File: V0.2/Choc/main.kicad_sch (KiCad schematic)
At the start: 41 parts, among them J1 Conn_01x02_Female, J1 USB_C_2.0, SW1 SW_DPST_x2, SW10 SW_DPST_x2, SW11 SW_DPST_x2, SW12 SW_DPST_x2, SW13 SW_DPST_x2, SW14 SW_DPST_x2, SW15 SW_DPST_x2, SW16 SW_DPST_x2, SW17 SW_DPST_x2, SW18 SW_DPST_x2, SW19 SW_DPST_x2, SW2 SW_DPST_x2, SW20 SW_DPST_x2, SW21 SW_DPST_x2, SW3 SW_DPST_x2, SW4 SW_DPST_x2, SW5 SW_DPST_x2, SW6 SW_DPST_x2, SW7 SW_DPST_x2, SW8 SW_DPST_x2, SW9 SW_DPST_x2, U1 E73-2G4M08S1E, X1 32.768kHz

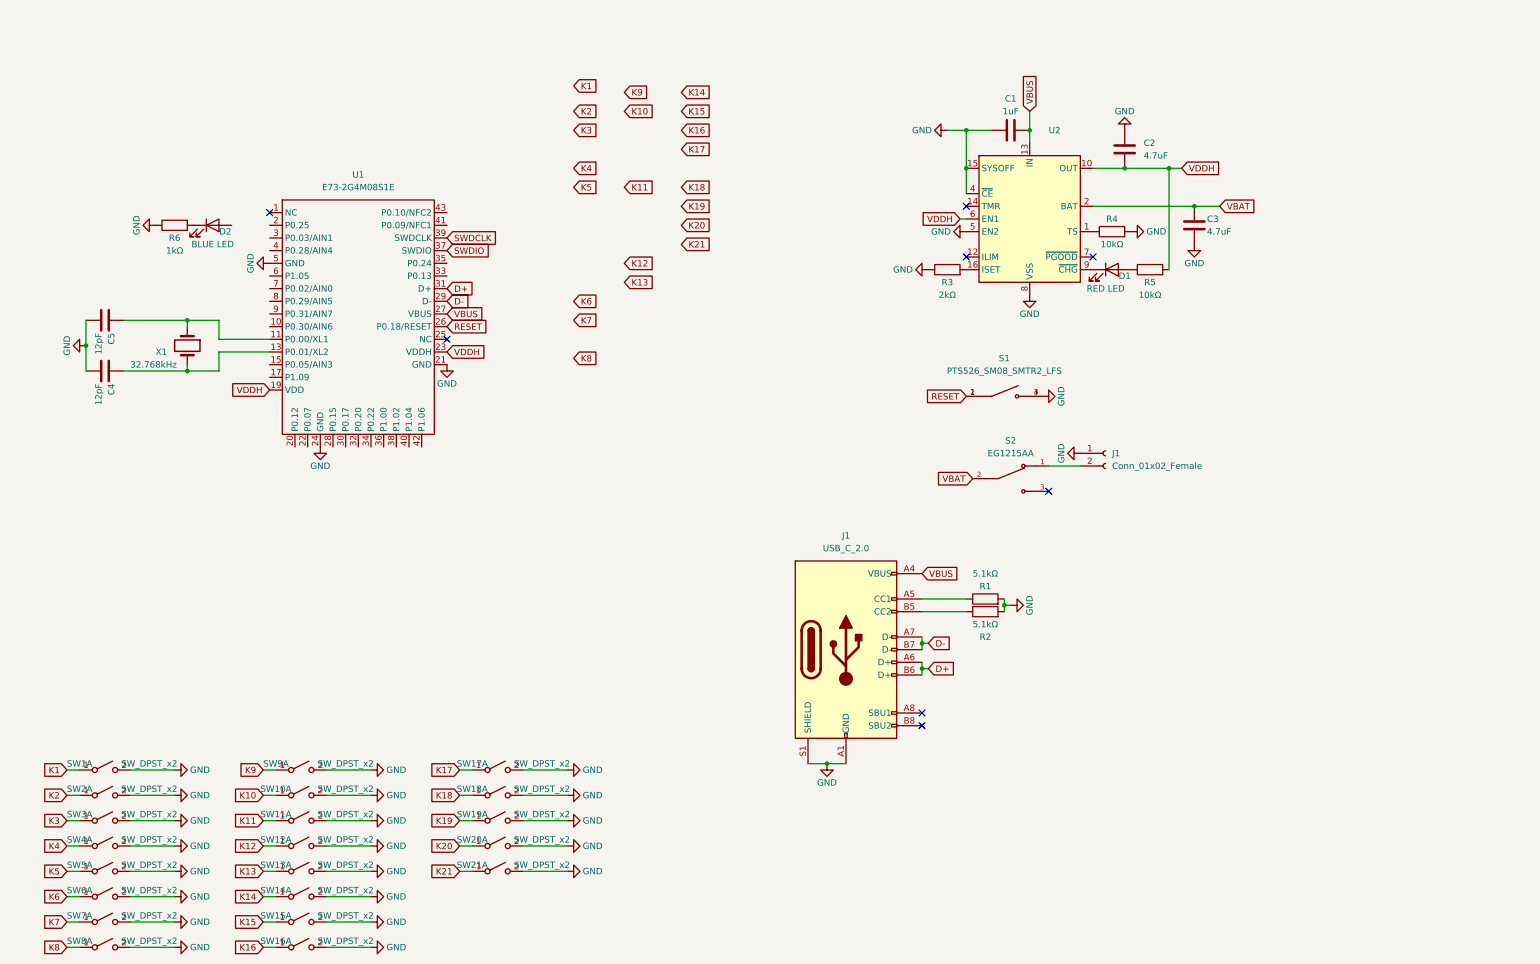
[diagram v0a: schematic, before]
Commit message: Just need to change ESD
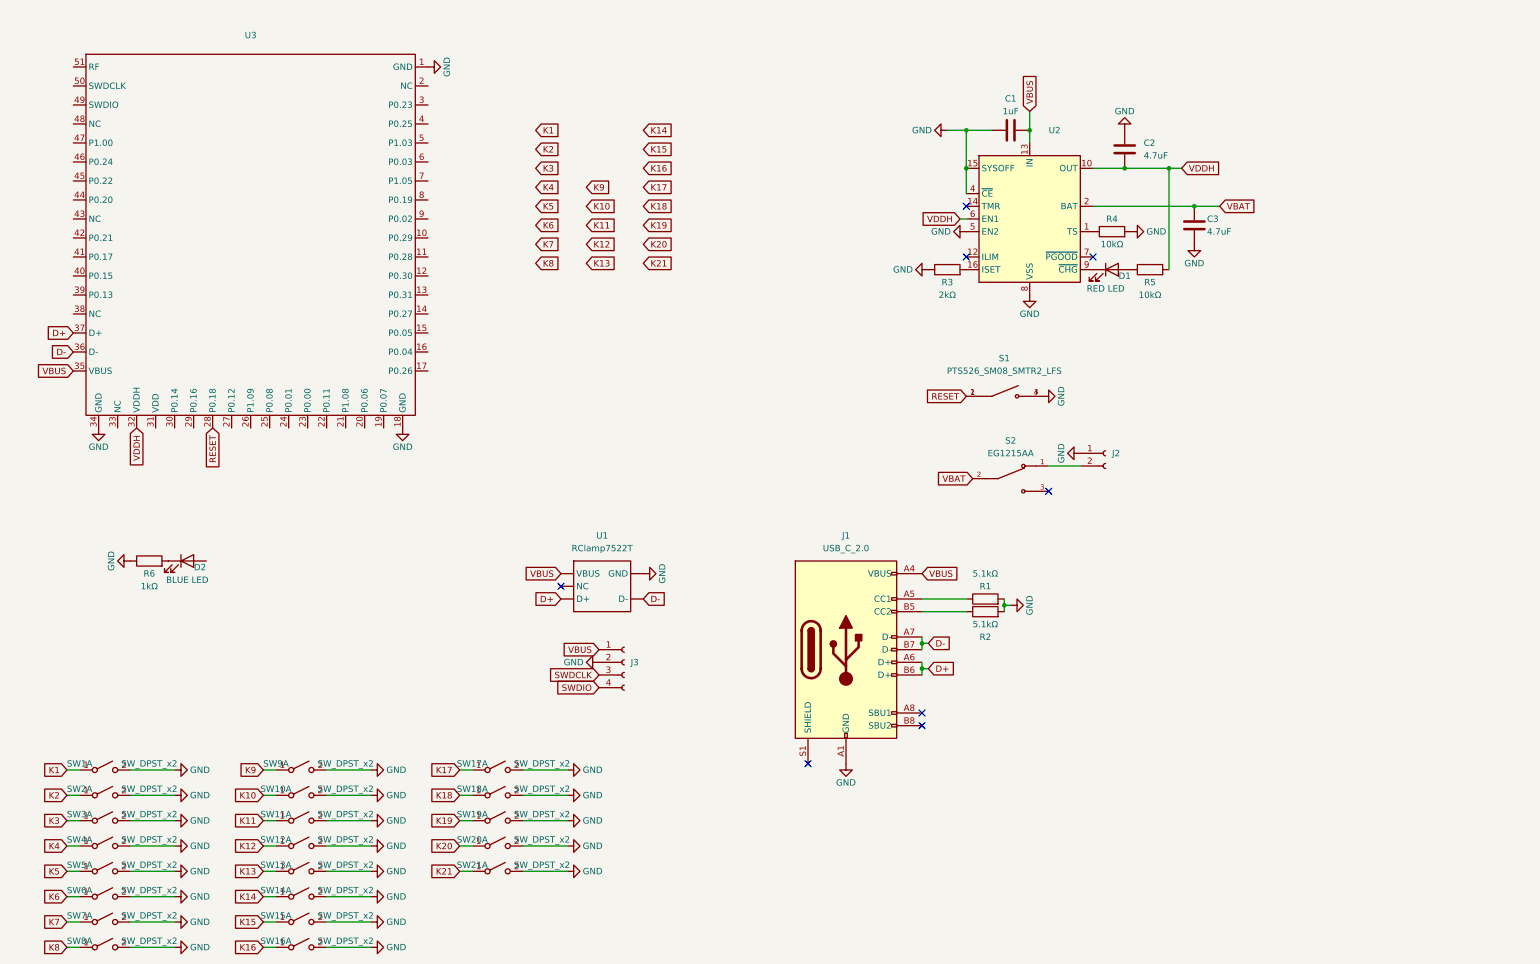
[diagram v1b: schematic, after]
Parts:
- removed C4, C5: 12pF, symbol Device:C
- removed U1: E73-2G4M08S1E, symbol E73-2G4M08S1E:E73-2G4M08S1E
- removed X1: 32.768kHz, symbol Device:Crystal
- added J3: (no value), symbol Connector:Conn_01x04_Female
- added U1: RClamp7522T, symbol Semtech:RClamp7522T
- added U3: (no value), symbol 0_ARognes:MS88SF31_Min
- J2: renamed from J1; value Conn_01x02_Female -> (none)
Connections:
- net D+: now also U1. (VBUS), U3.37 (D+)
- net D-: now also U1. (VBUS), U3.36 (D-)
- net GND: now also J3.2 (Pin_2), U1. (VBUS), U3.1 (GND), U3.18 (GND), U3.34 (GND); no longer J1.S1 (SHIELD)
- net RESET: now also U3.28 (P0.18)
- net SWDCLK: now also J3.3 (Pin_3)
- net SWDIO: now also J3.4 (Pin_4)
- net VBUS: now also J3.1 (Pin_1), U1. (VBUS), U3.35 (VBUS)
- net VDDH: now also U3.32 (VDDH)
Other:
- title: (none) -> Estoc

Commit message: Difficult circuitry complete, just wire
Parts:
- removed U1: RClamp7522T, symbol Semtech:RClamp7522T
- added U1: IP4234CZ6, symbol Nexperia:IP4234CZ6
- J2: value (none) -> JST-BAT
- J3: value (none) -> SWD
- U2: value (none) -> BQ24072; footprint (none) -> Package_DFN_QFN:VQFN-16-1EP_3x3mm_P0.5mm_EP1.6x1.6mm
- U3: value (none) -> MS88SF31_Min
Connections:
- net D+: now also U1.3 (ESD); no longer U3.37 (D+)
- net D-: now also U1.4 (ESD); no longer U3.36 (D-)
- net GND: now also U1.2 (GND)
- net SWDCLK: now also U3.50 (SWDCLK)
- net SWDIO: now also U3.49 (SWDIO)
- net VBUS: now also U1.5 (VBUS)
- net STATUS: now reaches D2.2 (A)
- new net D+ESD: U1.1 (ESD), U3.37 (D+)
- new net D-ESD: U1.6 (ESD), U3.36 (D-)
- no-connect marks 8 -> 14

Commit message: Update Readme
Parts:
- added C4: 1uF, symbol Device:C
- added C5, C6: 4.7uF, symbol Device:C
- added D3: RED LED, symbol Device:LED
- added D4: BLUE LED, symbol Device:LED
- added J4: USB_C_2.0, symbol Connector:USB_C_Receptacle_USB2.0
- added J5: JST-BAT, symbol Connector:Conn_01x02_Female
- added J6: SWD, symbol Connector:Conn_01x04_Female
- added R10, R11: 10kΩ, symbol Device:R
- added R12: 1kΩ, symbol Device:R
- added R7, R8: 5.1kΩ, symbol Device:R
- added R9: 2kΩ, symbol Device:R
- added S3: (no value), SW_PTS526_SM08_SMTR2_LFS, symbol PTS526_SM08_SMTR2_LFS:PTS526_SM08_SMTR2_LFS
- added S4: EG1215AA, SW_EG1215AA, symbol EG1215AA:EG1215AA
- added SW22, SW23, SW24, SW25, SW26, SW27, SW28, SW29, SW30, SW31, SW32, SW33, SW34, SW35, SW36, SW37, SW38, SW39, SW40, SW41, SW42: SW_DPST_x2, symbol Switch:SW_DPST_x2
- added U4: MS88SF31_Min, symbol 0_ARognes:MS88SF31_Min
- added U5: BQ24072, Package_DFN_QFN:VQFN-16-1EP_3x3mm_P0.5mm_EP1.6x1.6mm, symbol Battery_Management:BQ24075RGT
- added U6: IP4234CZ6, symbol Nexperia:IP4234CZ6
- S1: value PTS526_SM08_SMTR2_LFS -> (none)
- renumbered U3 to U1, U1 to U3
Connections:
- net D+: now also J4.A6 (D+), J4.B6 (D+), U6.3 (ESD)
- net D+ESD: now also U4.37 (D+), U6.1 (ESD)
- net D-: now also J4.A7 (D-), J4.B7 (D-), U6.4 (ESD)
- net D-ESD: now also U4.36 (D-), U6.6 (ESD)
- net GND: now also C4.1, C5.2, C6.1, J4.A1 (GND), J4.A12 (GND), J4.B1 (GND), J4.B12 (GND), J5.1 (Pin_1), J6.2 (Pin_2), R10.2, R12.1, R7.2, R8.2, R9.1, S3.3, S3.4, SW22.2 (B), SW23.2 (B), SW24.2 (B), SW25.2 (B), SW26.2 (B), SW27.2 (B), SW28.2 (B), SW29.2 (B), SW30.2 (B), SW31.2 (B), SW32.2 (B), SW33.2 (B), SW34.2 (B), SW35.2 (B), SW36.2 (B), SW37.2 (B), SW38.2 (B), SW39.2 (B), SW40.2 (B), SW41.2 (B), SW42.2 (B), U4.1 (GND), U4.18 (GND), U4.34 (GND), U5.15 (SYSOFF), U5.17 (VSS), U5.4 (~{CE}), U5.5 (EN2), U5.8 (VSS), U6.2 (GND)
- net K1: now also U1.23 (P0.00), SW22.1 (A), U4.20 (P0.06)
- net K10: now also U1.29 (P0.16), SW31.1 (A), U4.11 (P0.28)
- net K11: now also U1.40 (P0.15), SW32.1 (A), U4.10 (P0.29)
- net K12: now also U1.44 (P0.20), SW33.1 (A), U4.3 (P0.23)
- net K13: now also U1.20 (P0.06), SW34.1 (A), U4.25 (P0.08)
- net K14: now also U1.19 (P0.07), SW35.1 (A), U4.39 (P0.13)
- net K15: now also U1.16 (P0.04), SW36.1 (A), U4.40 (P0.15)
- net K16: now also U1.15 (P0.05), SW37.1 (A), U4.41 (P0.17)
- net K17: now also U1.24 (P0.01), SW38.1 (A), U4.42 (P0.21)
- net K18: now also U1.39 (P0.13), SW39.1 (A), U4.5 (P1.03)
- net K19: now also U1.5 (P1.03), SW40.1 (A), U4.45 (P0.22)
- net K2: now also U1.26 (P1.09), SW23.1 (A), U4.21 (P1.08)
- net K20: now also U1.4 (P0.25), SW41.1 (A), U4.46 (P0.24)
- net K21: now also U1.3 (P0.23), SW42.1 (A), U4.47 (P1.00)
- net K3: now also U1.27 (P0.12), SW24.1 (A), U4.13 (P0.31)
- net K4: now also U1.30 (P0.14), SW25.1 (A), U4.12 (P0.30)
- net K5: now also U1.41 (P0.17), SW26.1 (A), U4.9 (P0.02)
- net K6: now also U1.42 (P0.21), SW27.1 (A), U4.4 (P0.25)
- net K7: now also U1.22 (P0.11), SW28.1 (A), U4.23 (P0.00)
- net K8: now also U1.21 (P1.08), SW29.1 (A), U4.24 (P0.01)
- net K9: now also U1.25 (P0.08), SW30.1 (A), U4.22 (P0.11)
- net RESET: now also S3.1, S3.2, U4.28 (P0.18)
- net STATUS: now also U1.17 (P0.26), D4.2 (A), U4.17 (P0.26)
- net SWDCLK: now also J6.3 (Pin_3), U4.50 (SWDCLK)
- net SWDIO: now also J6.4 (Pin_4), U4.49 (SWDIO)
- net VBAT: now also C6.2, S4.2, U5.2 (BAT), U5.3 (BAT)
- net VBUS: now also C4.2, J4.A4 (VBUS), J4.A9 (VBUS), J4.B4 (VBUS), J4.B9 (VBUS), J6.1 (Pin_1), U4.35 (VBUS), U5.13 (IN), U6.5 (VBUS)
- net VDDH: now also C5.1, R11.2, U4.32 (VDDH), U5.10 (OUT), U5.11 (OUT), U5.6 (EN1)
- new net: J5.2 (Pin_2), S4.1
- new net: R9.2, U5.16 (ISET)
- new net: J4.A5 (CC1), R7.1
- new net: D3.2 (A), R11.1
- new net: R10.1, U5.1 (TS)
- new net: D3.1 (K), U5.9 (~{CHG})
- new net: D4.1 (K), R12.2
- new net: J4.B5 (CC2), R8.1
- no-connect marks 14 -> 51
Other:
- note added: "Key Switches"
- note added: "Microprocessor"
- note added: "On/Off Switch"
- note added: "Power Circuit"
- note added: "Reset Button"
- note added: "SWD"
- note added: "Status LED"
- note added: "USB 2.0"
- note added: "USB 2.0 ESD Protection"
- moved on the sheet: C1, C2, C3, D1, D2, J1, J2, J3, R1, R2, R3, R4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

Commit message: Sent to pcbway
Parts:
- R3, R9: value 2kΩ -> (none)
- R5: value 10kΩ -> (none)
- R6: value 1kΩ -> (none)
- S1, S3: value (none) -> TL3330AF260QG
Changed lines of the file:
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@@
     (in_bom yes) (on_board yes)
     (property "Reference" "R9" (id 0) (at 254 55.88 90))
-    (property "Value" "2kΩ" (id 1) (at 254 58.42 90))
+    (property "Value" "" (id 1) (at 254 58.42 90))
     (property "Footprint" "" (id 2) (at 254 55.118 90)
       (effects (font (size 1.27 1.27)) hide)
@@
     (in_bom yes) (on_board yes)
     (property "Reference" "R3" (id 0) (at 101.6 55.88 90))
-    (property "Value" "2kΩ" (id 1) (at 101.6 58.42 90))
+    (property "Value" "" (id 1) (at 101.6 58.42 90))
     (property "Footprint" "" (id 2) (at 101.6 55.118 90)
       (effects (font (size 1.27 1.27)) hide)
@@
     (in_bom yes) (on_board yes)
     (property "Reference" "R6" (id 0) (at 119.38 78.74 90))
-    (property "Value" "1kΩ" (id 1) (at 119.38 81.28 90))
+    (property "Value" "" (id 1) (at 119.38 81.28 90))
     (property "Footprint" "" (id 2) (at 119.38 77.978 90)
       (effects (font (size 1.27 1.27)) hide)
@@
     (in_bom yes) (on_board yes)
     (property "Reference" "R5" (id 0) (at 142.24 55.88 90))
-    (property "Value" "10kΩ" (id 1) (at 142.24 58.42 90))
+    (property "Value" "" (id 1) (at 142.24 58.42 90))
     (property "Footprint" "" (id 2) (at 142.24 55.118 90)
       (effects (font (size 1.27 1.27)) hide)
@@
     (in_bom yes) (on_board yes)
     (property "Reference" "S3" (id 0) (at 173.99 92.71 0))
-    (property "Value" "" (id 1) (at 190.5 92.71 0))
+    (property "Value" "TL3330AF260QG" (id 1) (at 190.5 92.71 0))
     (property "Footprint" "SW_PTS526_SM08_SMTR2_LFS" (id 2) (at 190.5 97.79 0)
       (effects (font (size 1.27 1.27)) (justify left bottom) hide)
@@
     (in_bom yes) (on_board yes)
     (property "Reference" "S1" (id 0) (at 19.05 92.71 0))
-    (property "Value" "" (id 1) (at 34.29 92.71 0))
+    (property "Value" "TL3330AF260QG" (id 1) (at 34.29 92.71 0))
     (property "Footprint" "SW_PTS526_SM08_SMTR2_LFS" (id 2) (at 34.29 97.79 0)
       (effects (font (size 1.27 1.27)) (justify left bottom) hide)
@@
     )
     (path "/239e21bd-773b-4fee-abfc-ec5197a2b619"
-      (reference "R3") (unit 1) (value "2kΩ") (footprint "")
+      (reference "R3") (unit 1) (value "10kΩ") (footprint "")
     )
     (path "/d52873d9-d07b-40ed-950f-a226784070f7"
@@
     )
     (path "/986e13fd-842d-4ea0-bb4c-ff66ffd60a21"
-      (reference "R5") (unit 1) (value "10kΩ") (footprint "")
+      (reference "R5") (unit 1) (value "480Ω") (footprint "")
     )
     (path "/788adcf3-3377-42ef-891d-7a2c80072b93"
-      (reference "R6") (unit 1) (value "1kΩ") (footprint "")
+      (reference "R6") (unit 1) (value "55Ω") (footprint "")
     )
     (path "/2413847e-2c93-4fcd-97a5-d54627bc5033"
@@
     )
     (path "/11557e62-41e9-41b1-8e74-41c05c983d9f"
-      (reference "R9") (unit 1) (value "2kΩ") (footprint "")
+      (reference "R9") (unit 1) (value "10kΩ") (footprint "")
     )
     (path "/6d77d19c-aefc-4e74-b12e-40b1567a9bfc"
